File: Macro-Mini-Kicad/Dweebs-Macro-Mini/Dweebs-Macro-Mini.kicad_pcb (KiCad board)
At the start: 2 copper layers, 57 parts, among them U1 ProMicro

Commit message: Final for proto
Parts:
- D1, D10, D11, D12, D13, D14, D15, D16, D17, D18, D19, D2, D20, D21, D22, D23, D24, D25, D26, D27, D28, D3, D4, D5, D6, D7, D8, D9: moved to B.Cu
- moved D8 187.5 mm to (91.3, 70.6), turned to 90 degrees
- moved D14 175.6 mm to (91.3, 89.7), turned to 90 degrees
- moved D15 173.8 mm to (110.3, 89.7), turned to 90 degrees
- moved D9 163.1 mm to (110.3, 70.6), turned to 90 degrees
- moved D20 160.1 mm to (91.3, 108.7), turned to 90 degrees
- moved D4 140.1 mm to (148.4, 51.6), turned to 90 degrees
- moved D10 138.0 mm to (130.2, 70.6), turned to 90 degrees
- moved D26 131.7 mm to (138.1, 130.2), turned to 90 degrees
- moved D21 129.4 mm to (110.3, 108.7), turned to 90 degrees
- moved D11 124.8 mm to (148.4, 70.6), turned to 90 degrees
- moved D27 123.5 mm to (156.4, 138.1), turned to 90 degrees
- moved D22 116.3 mm to (129.4, 108.7), turned to 90 degrees
- moved D5 116.2 mm to (167.5, 51.6), turned to 90 degrees
- moved D16 114.8 mm to (129.4, 89.7), turned to 90 degrees
- moved D23 110.0 mm to (148.4, 108.7), turned to 90 degrees
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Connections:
- U1 pad 10: Net-(U1-Pad10) -> COL4
- U1 pad 11: Net-(U1-Pad11) -> COL5
- U1 pad 12: Net-(U1-Pad12) -> COL6
- U1 pad 15: Net-(U1-Pad15) -> ROW4
- U1 pad 16: Net-(U1-Pad16) -> ROW3
- U1 pad 17: Net-(U1-Pad17) -> ROW2
- U1 pad 18: Net-(U1-Pad18) -> ROW1
- U1 pad 19: Net-(U1-Pad19) -> ROW0
- U1 pad 20: Net-(U1-Pad20) -> COL0
- U1 pad 7: Net-(U1-Pad7) -> COL1
- U1 pad 8: Net-(U1-Pad8) -> COL2
- U1 pad 9: Net-(U1-Pad9) -> COL3
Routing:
- net COL3: track 0.00 -> 394.2 mm
- net COL5: track 0.00 -> 386.4 mm
- net COL2: track 0.00 -> 192.7 mm
- net COL6: track 0.00 -> 185.0 mm
- net ROW0: track 0.00 -> 178.8 mm
- net COL4: track 0.00 -> 159.8 mm
- net COL1: track 0.00 -> 159.7 mm
- net ROW1: track 0.00 -> 152.9 mm
- net COL0: track 0.00 -> 130.3 mm
- net ROW2: track 0.00 -> 129.2 mm
- net ROW3: track 0.00 -> 109.7 mm
- net ROW4: track 0.00 -> 80.7 mm
- net Net-(D28-Pad2): track 0.00 -> 10.4 mm
- net Net-(D27-Pad2): track 0.00 -> 8.95 mm
- net Net-(D10-Pad2): track 0.00 -> 8.40 mm
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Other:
- board outline added: 133.3 x 111.1 mm
- board text added: "Dweebs Macro Mini By: Keyboard Dweebs"

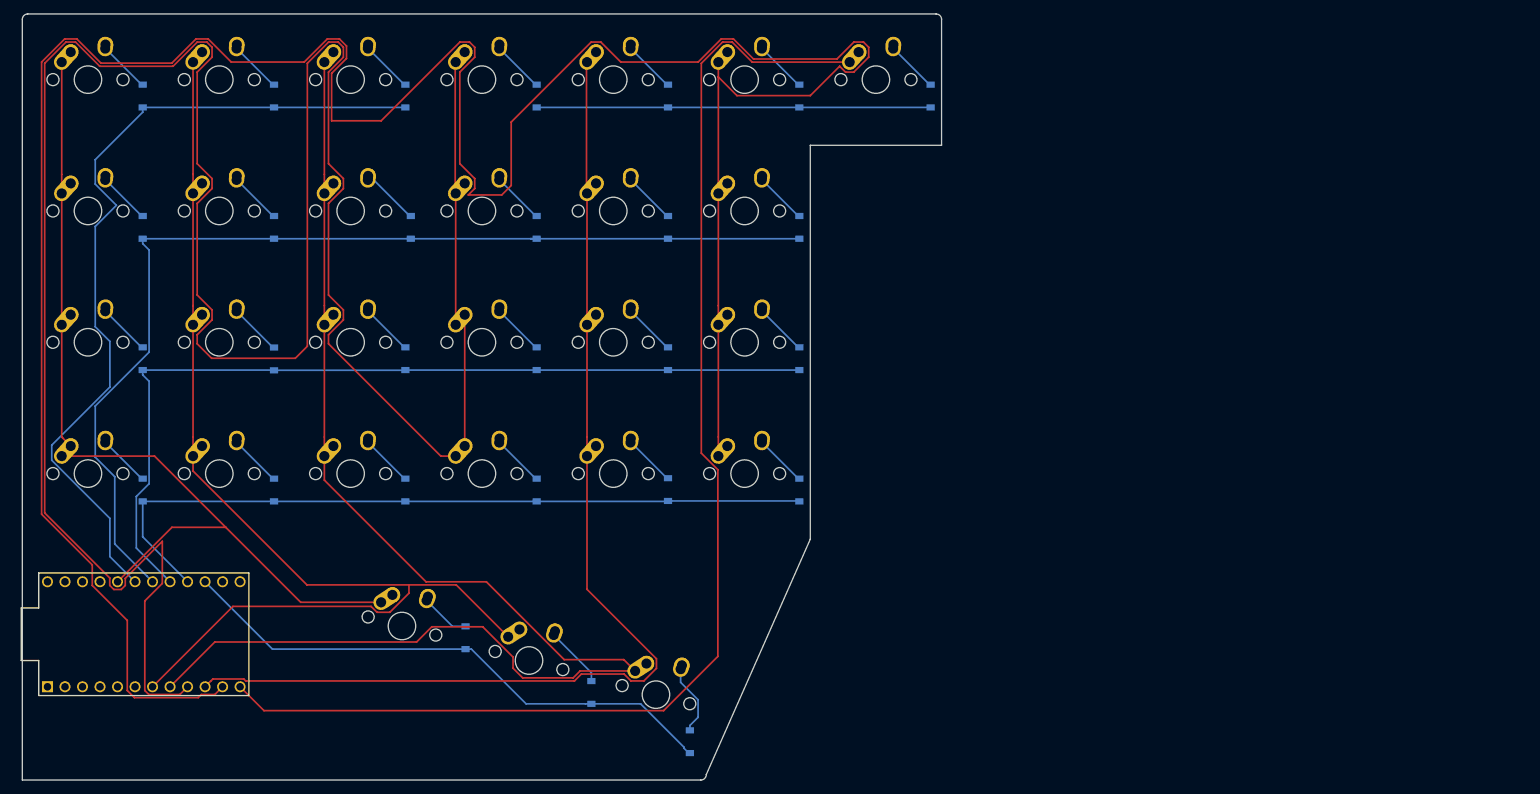
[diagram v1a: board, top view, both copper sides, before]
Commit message: remade vias
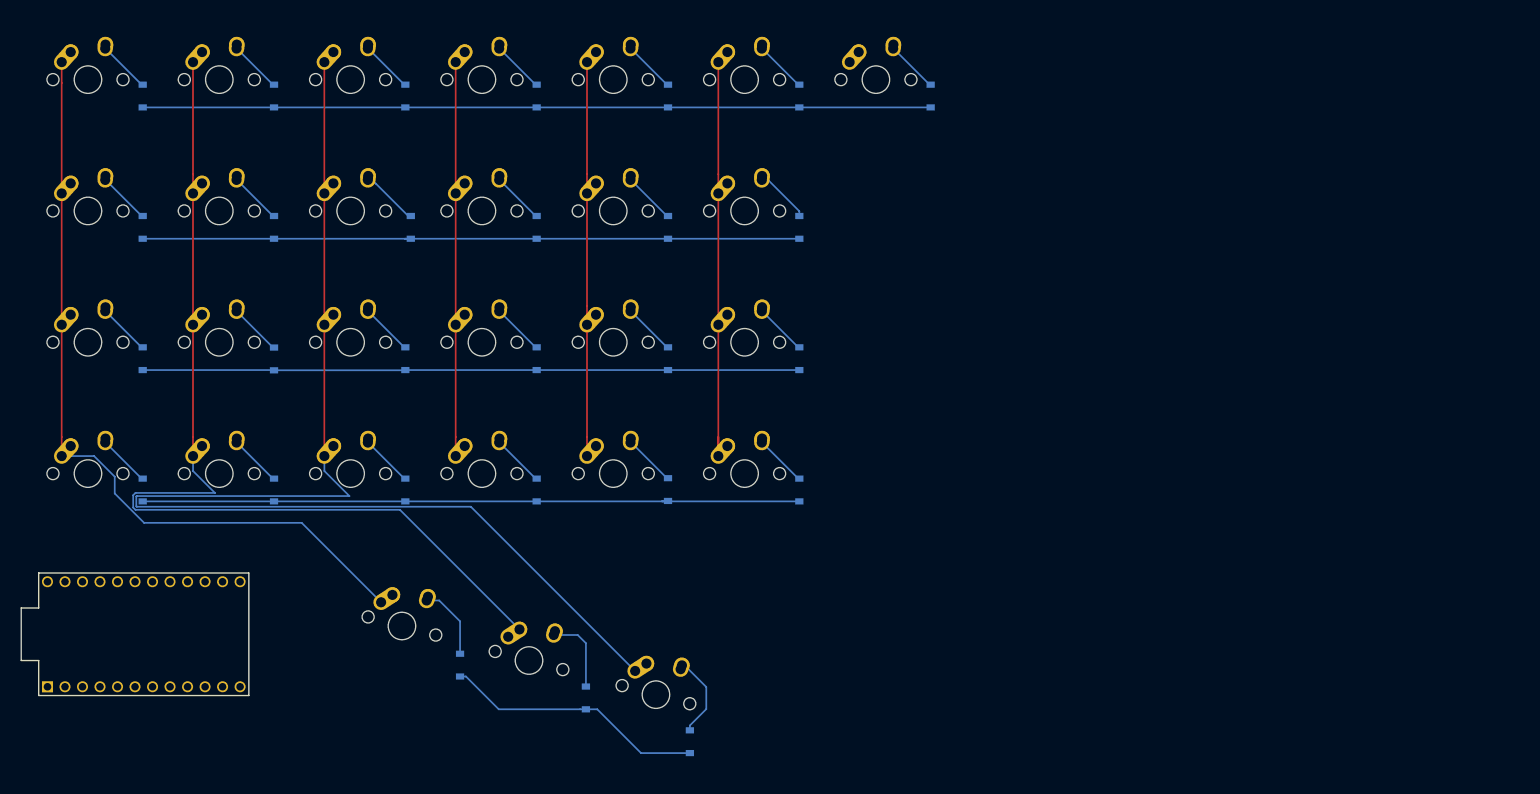
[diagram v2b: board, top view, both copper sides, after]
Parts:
- moved D26 4.05 mm to (137.3, 134.1)
- moved D27 1.12 mm to (155.6, 138.9)
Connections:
- U1 pad 10: COL4 -> Net-(U1-Pad10)
- U1 pad 11: COL5 -> Net-(U1-Pad11)
- U1 pad 12: COL6 -> Net-(U1-Pad12)
- U1 pad 13: Net-(U1-Pad13) -> ROW4
- U1 pad 14: Net-(U1-Pad14) -> ROW3
- U1 pad 15: ROW4 -> ROW2
- U1 pad 16: ROW3 -> ROW1
- U1 pad 17: ROW2 -> ROW0
- U1 pad 18: ROW1 -> Net-(U1-Pad18)
- U1 pad 19: ROW0 -> Net-(U1-Pad19)
- U1 pad 20: COL0 -> Net-(U1-Pad20)
- U1 pad 7: COL1 -> Net-(U1-Pad7)
- U1 pad 8: COL2 -> Net-(U1-Pad8)
- U1 pad 9: COL3 -> Net-(U1-Pad9)
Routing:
- net COL3: track 394.2 -> 57.2 mm
- net COL5: track 386.4 -> 59.9 mm
- net COL6: track 185.0 -> 0.00 mm
- net COL4: track 159.8 -> 57.2 mm
- net ROW0: track 178.8 -> 114.3 mm
- net ROW1: track 152.9 -> 96.1 mm
- net ROW4: track 80.7 -> 37.9 mm
- net ROW2: track 129.2 -> 95.3 mm
- net COL1: track 159.7 -> 141.0 mm
- net COL0: track 130.3 -> 113.7 mm
- net COL2: track 192.7 -> 179.1 mm
- net ROW3: track 109.7 -> 96.1 mm
- net Net-(D26-Pad2): track 7.20 -> 10.8 mm
- net Net-(D27-Pad2): track 8.95 -> 11.5 mm
- net Net-(D28-Pad2): track 10.4 -> 12.1 mm
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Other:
- board outline removed
- board text removed: "Dweebs Macro Mini By: Keyboard Dweebs"

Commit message: trace reroute
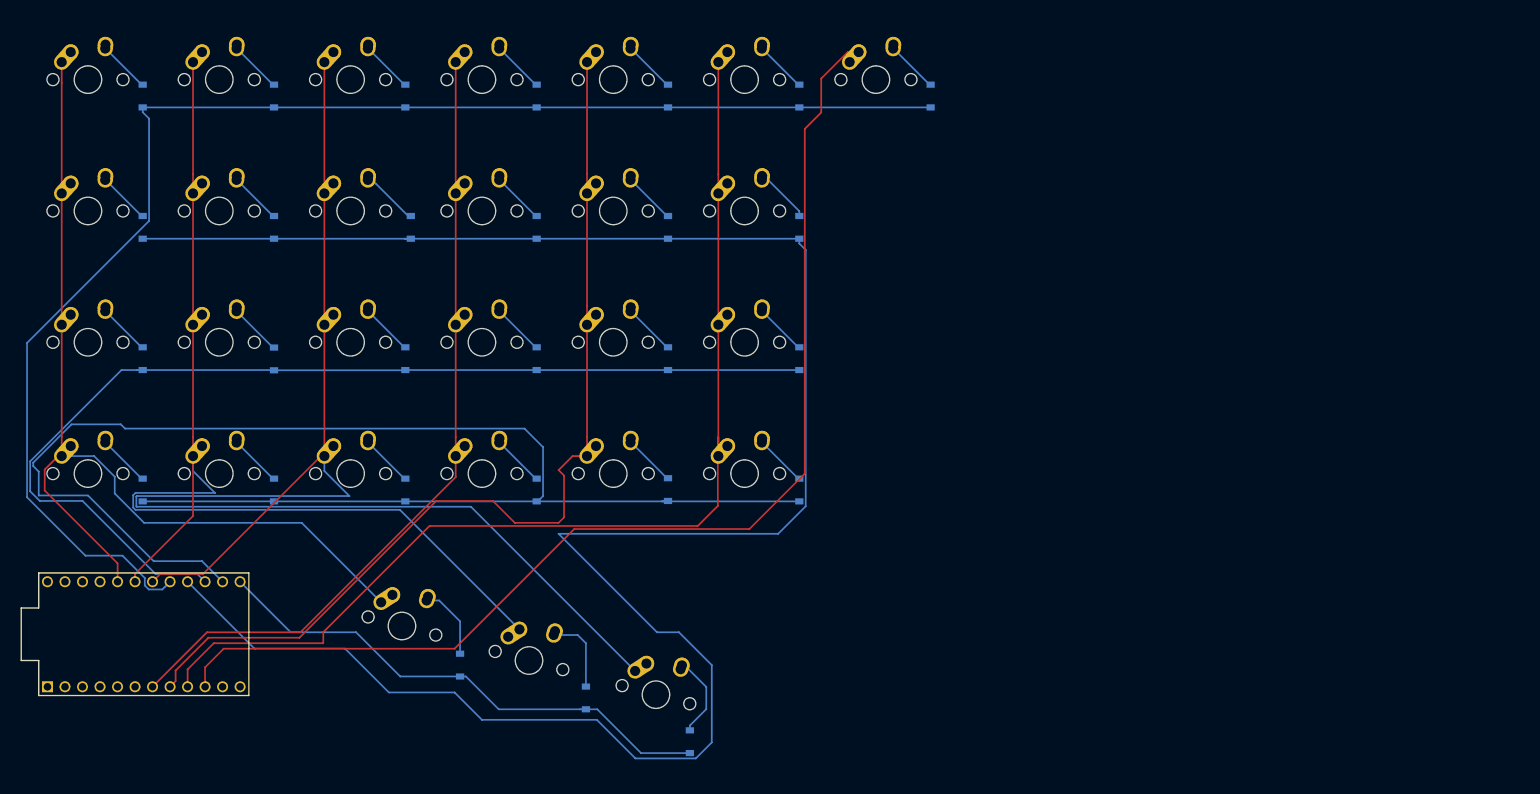
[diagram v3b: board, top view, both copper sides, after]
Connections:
- U1 pad 10: Net-(U1-Pad10) -> COL6
- U1 pad 18: Net-(U1-Pad18) -> COL2
- U1 pad 19: Net-(U1-Pad19) -> COL1
- U1 pad 20: Net-(U1-Pad20) -> COL0
- U1 pad 7: Net-(U1-Pad7) -> COL3
- U1 pad 8: Net-(U1-Pad8) -> COL4
- U1 pad 9: Net-(U1-Pad9) -> COL5
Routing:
- net ROW1: track 96.1 -> 301.8 mm
- net COL6: track 0.00 -> 166.8 mm
- net ROW3: track 96.1 -> 219.0 mm
- net COL5: track 59.9 -> 157.4 mm
- net ROW0: track 114.3 -> 206.0 mm
- net COL4: track 57.2 -> 140.2 mm
- net COL3: track 57.2 -> 116.8 mm
- net ROW2: track 95.3 -> 152.2 mm
- net ROW4: track 37.9 -> 75.5 mm
- net COL2: track 179.1 -> 211.5 mm
- net COL0: track 113.7 -> 137.6 mm
- net COL1: track 141.0 -> 162.7 mm

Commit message: silkscreen
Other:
- board outline added: 133.3 x 111.1 mm
- board text added: "Dweebs Macro Mini By: Keyboard Dweebs"
- board text added: "RAW"
- board text added: "TX"
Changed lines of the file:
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@@
   (general
     (thickness 1.6)
-    (drawings 0)
+    (drawings 10)
     (tracks 277)
     (zones 0)
@@
     )
   )
+  (gr_text "Dweebs Macro Mini\nBy: Keyboard Dweebs" (at 91.28125 144.4625) (layer F.SilkS)
+    (effects (font (size 2 2) (thickness 0.15)))
+  )
+  (gr_text RAW (at 77.7875 124.61875 90) (layer B.SilkS)
+    (effects (font (size 0.5 0.5) (thickness 0.125)) (justify mirror))
+  )
+  (gr_text TX (at 77.7875 134.9375 90) (layer B.SilkS)
+    (effects (font (size 0.5 0.5) (thickness 0.125)) (justify mirror))
+  )
+  (gr_line (start 188.11875 58.7375) (end 188.11875 115.8875) (layer Edge.Cuts) (width 0.05))
+  (gr_line (start 207.16875 58.7375) (end 188.11875 58.7375) (layer Edge.Cuts) (width 0.05))
+  (gr_line (start 207.16875 39.6875) (end 207.16875 58.7375) (layer Edge.Cuts) (width 0.05))
+  (gr_line (start 73.81875 39.6875) (end 207.16875 39.6875) (layer Edge.Cuts) (width 0.05))
+  (gr_line (start 73.81875 150.8125) (end 73.81875 39.6875) (layer Edge.Cuts) (width 0.05))
+  (gr_line (start 172.24375 150.8125) (end 73.81875 150.8125) (layer Edge.Cuts) (width 0.05))
+  (gr_line (start 188.11875 115.8875) (end 172.24375 150.8125) (layer Edge.Cuts) (width 0.05))
   (segment (start 85.9 44.7125) (end 85.84375 44.7125) (width 0.25) (layer B.Cu) (net 1))
   (segment (start 91.13125 49.94375) (end 85.9 44.7125) (width 0.25) (layer B.Cu) (net 1))
